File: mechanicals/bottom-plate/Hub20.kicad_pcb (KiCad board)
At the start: 4 copper layers, 89 x 124 mm, 4 parts

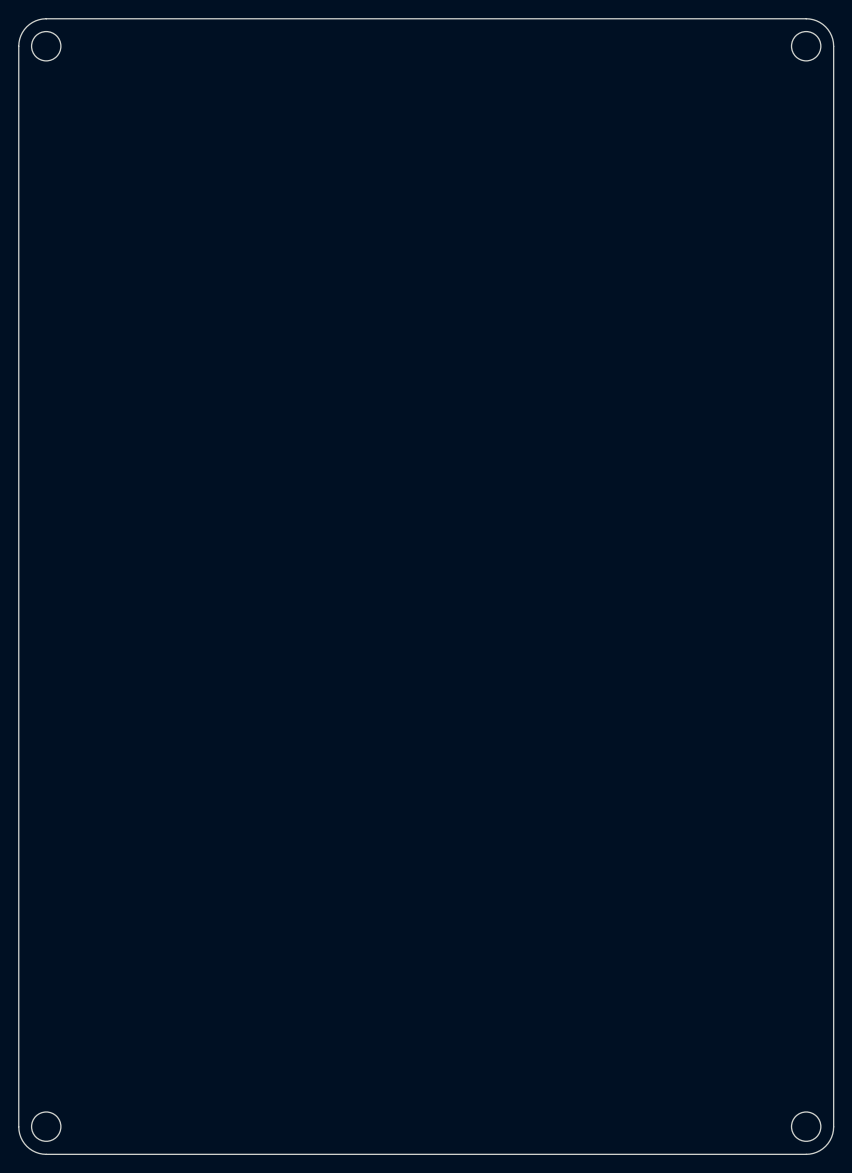
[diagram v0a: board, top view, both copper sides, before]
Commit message: limit 2U to 3 pin only
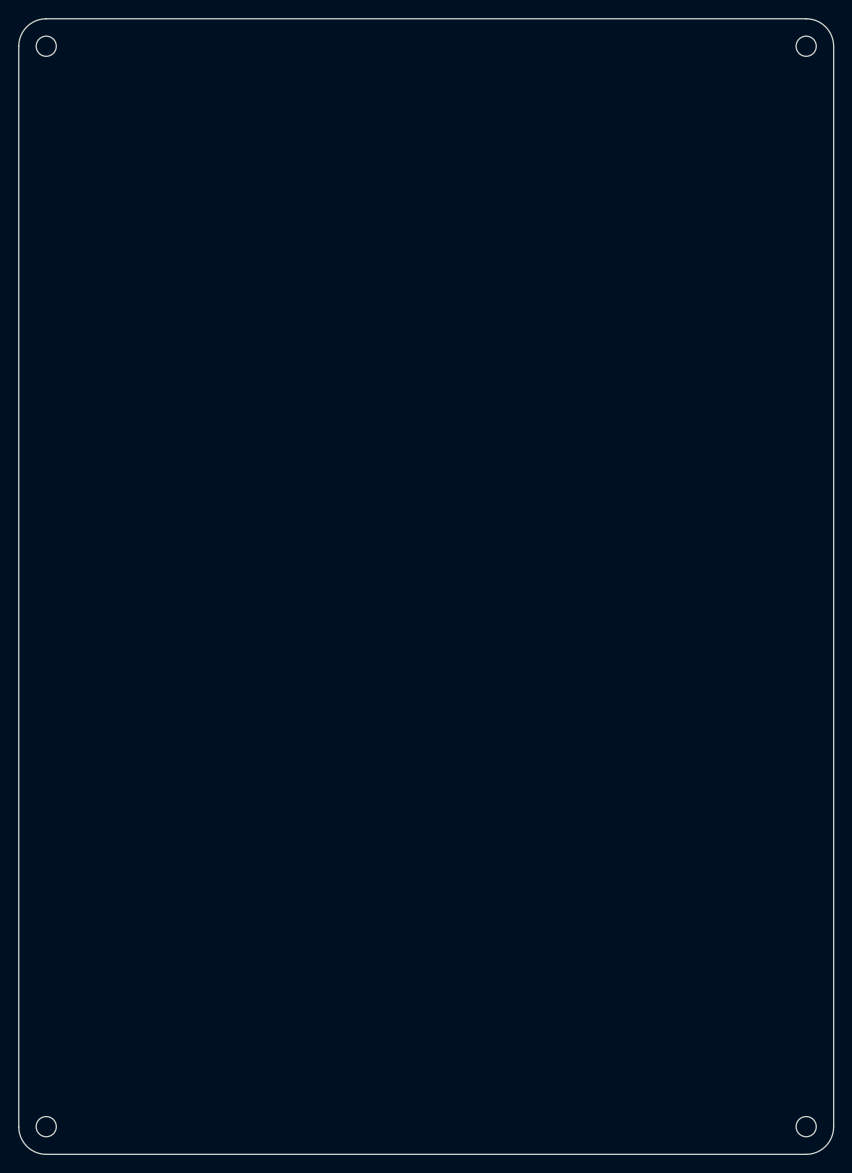
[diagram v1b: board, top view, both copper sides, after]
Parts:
- H1, H2, H3, H4: footprint MountingHole:MountingHole_3.2mm_M3 -> MountingHole:MountingHole_2.2mm_M2
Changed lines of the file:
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@@
-(kicad_pcb (version 20171130) (host pcbnew 5.1.6-c6e7f7d~87~ubuntu20.04.1)
+(kicad_pcb (version 20171130) (host pcbnew "(5.1.5)-3")
   (general
     (thickness 1.6)
@@
     (diff_pair_gap 0.2)
   )
-  (module MountingHole:MountingHole_3.2mm_M3 locked (layer F.Cu)
+  (module MountingHole:MountingHole_2.2mm_M2 locked (layer F.Cu)
     (at 180.45 157.5375)
-    (descr "Mounting Hole 3.2mm, no annular, M3")
-    (tags "mounting hole 3.2mm no annular m3")
+    (descr "Mounting Hole 2.2mm, no annular, M2")
+    (tags "mounting hole 2.2mm no annular m2")
     (attr virtual)
     (fp_text reference H3 (at 0 -4.2) (layer F.SilkS) hide
@@
       (effects (font (size 1 1) (thickness 0.15)))
     )
-    (fp_circle (center 0 0) (end 3.45 0) (layer F.CrtYd) (width 0.05))
-    (fp_circle (center 0 0) (end 3.2 0) (layer Cmts.User) (width 0.15))
+    (fp_circle (center 0 0) (end 2.45 0) (layer F.CrtYd) (width 0.05))
+    (fp_circle (center 0 0) (end 2.2 0) (layer Cmts.User) (width 0.15))
     (fp_text user %R (at 0.3 0) (layer F.Fab) hide
       (effects (font (size 1 1) (thickness 0.15)))
     )
-    (pad 1 np_thru_hole circle (at 0 0) (size 3.2 3.2) (drill 3.2) (layers *.Cu *.Mask))
-  )
-  (module MountingHole:MountingHole_3.2mm_M3 locked (layer F.Cu)
+    (pad 1 np_thru_hole circle (at 0 0) (size 2.2 2.2) (drill 2.2) (layers *.Cu *.Mask))
+  )
+  (module MountingHole:MountingHole_2.2mm_M2 locked (layer F.Cu)
     (at 97.45 157.5375)
-    (descr "Mounting Hole 3.2mm, no annular, M3")
-    (tags "mounting hole 3.2mm no annular m3")
+    (descr "Mounting Hole 2.2mm, no annular, M2")
+    (tags "mounting hole 2.2mm no annular m2")
     (attr virtual)
     (fp_text reference H4 (at 0 -4.2) (layer F.SilkS) hide
@@
       (effects (font (size 1 1) (thickness 0.15)))
     )
-    (fp_circle (center 0 0) (end 3.45 0) (layer F.CrtYd) (width 0.05))
-    (fp_circle (center 0 0) (end 3.2 0) (layer Cmts.User) (width 0.15))
+    (fp_circle (center 0 0) (end 2.45 0) (layer F.CrtYd) (width 0.05))
+    (fp_circle (center 0 0) (end 2.2 0) (layer Cmts.User) (width 0.15))
     (fp_text user %R (at 0.3 0) (layer F.Fab) hide
       (effects (font (size 1 1) (thickness 0.15)))
     )
-    (pad 1 np_thru_hole circle (at 0 0) (size 3.2 3.2) (drill 3.2) (layers *.Cu *.Mask))
-  )
-  (module MountingHole:MountingHole_3.2mm_M3 locked (layer F.Cu)
+    (pad 1 np_thru_hole circle (at 0 0) (size 2.2 2.2) (drill 2.2) (layers *.Cu *.Mask))
+  )
+  (module MountingHole:MountingHole_2.2mm_M2 locked (layer F.Cu)
     (at 180.45 39.5375 90)
-    (descr "Mounting Hole 3.2mm, no annular, M3")
-    (tags "mounting hole 3.2mm no annular m3")
+    (descr "Mounting Hole 2.2mm, no annular, M2")
+    (tags "mounting hole 2.2mm no annular m2")
     (attr virtual)
     (fp_text reference H1 (at 0 -4.2 90) (layer F.SilkS) hide
@@
       (effects (font (size 1 1) (thickness 0.15)))
     )
-    (fp_circle (center 0 0) (end 3.2 0) (layer Cmts.User) (width 0.15))
-    (fp_circle (center 0 0) (end 3.45 0) (layer F.CrtYd) (width 0.05))
+    (fp_circle (center 0 0) (end 2.45 0) (layer F.CrtYd) (width 0.05))
+    (fp_circle (center 0 0) (end 2.2 0) (layer Cmts.User) (width 0.15))
     (fp_text user %R (at 0.3 0 90) (layer F.Fab) hide
       (effects (font (size 1 1) (thickness 0.15)))
     )
-    (pad 1 np_thru_hole circle (at 0 0 90) (size 3.2 3.2) (drill 3.2) (layers *.Cu *.Mask))
-  )
-  (module MountingHole:MountingHole_3.2mm_M3 locked (layer F.Cu)
+    (pad 1 np_thru_hole circle (at 0 0 90) (size 2.2 2.2) (drill 2.2) (layers *.Cu *.Mask))
+  )
+  (module MountingHole:MountingHole_2.2mm_M2 locked (layer F.Cu)
     (at 97.45 39.5375)
-    (descr "Mounting Hole 3.2mm, no annular, M3")
-    (tags "mounting hole 3.2mm no annular m3")
+    (descr "Mounting Hole 2.2mm, no annular, M2")
+    (tags "mounting hole 2.2mm no annular m2")
     (attr virtual)
     (fp_text reference H2 (at 0 -4.2) (layer F.SilkS) hide
@@
       (effects (font (size 1 1) (thickness 0.15)))
     )
-    (fp_circle (center 0 0) (end 3.2 0) (layer Cmts.User) (width 0.15))
-    (fp_circle (center 0 0) (end 3.45 0) (layer F.CrtYd) (width 0.05))
+    (fp_circle (center 0 0) (end 2.45 0) (layer F.CrtYd) (width 0.05))
+    (fp_circle (center 0 0) (end 2.2 0) (layer Cmts.User) (width 0.15))
     (fp_text user %R (at 0.3 0) (layer F.Fab) hide
       (effects (font (size 1 1) (thickness 0.15)))
     )
-    (pad 1 np_thru_hole circle (at 0 0) (size 3.2 3.2) (drill 3.2) (layers *.Cu *.Mask))
+    (pad 1 np_thru_hole circle (at 0 0) (size 2.2 2.2) (drill 2.2) (layers *.Cu *.Mask))
   )
   (gr_line (start 94.45 157.5625) (end 94.45 39.5375) (layer Edge.Cuts) (width 0.1))
